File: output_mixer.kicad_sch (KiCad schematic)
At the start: 112 parts, among them J1 Conn_01x10, J11 IN2, J2 IN1, J3 IN1, J4 IN2, J5 Line out, J6 Headphones, Q2 BD139, Q3 BD140, Q4 BD139, Q5 BD140, U1 TL072, U2 TL072, U3 TL072

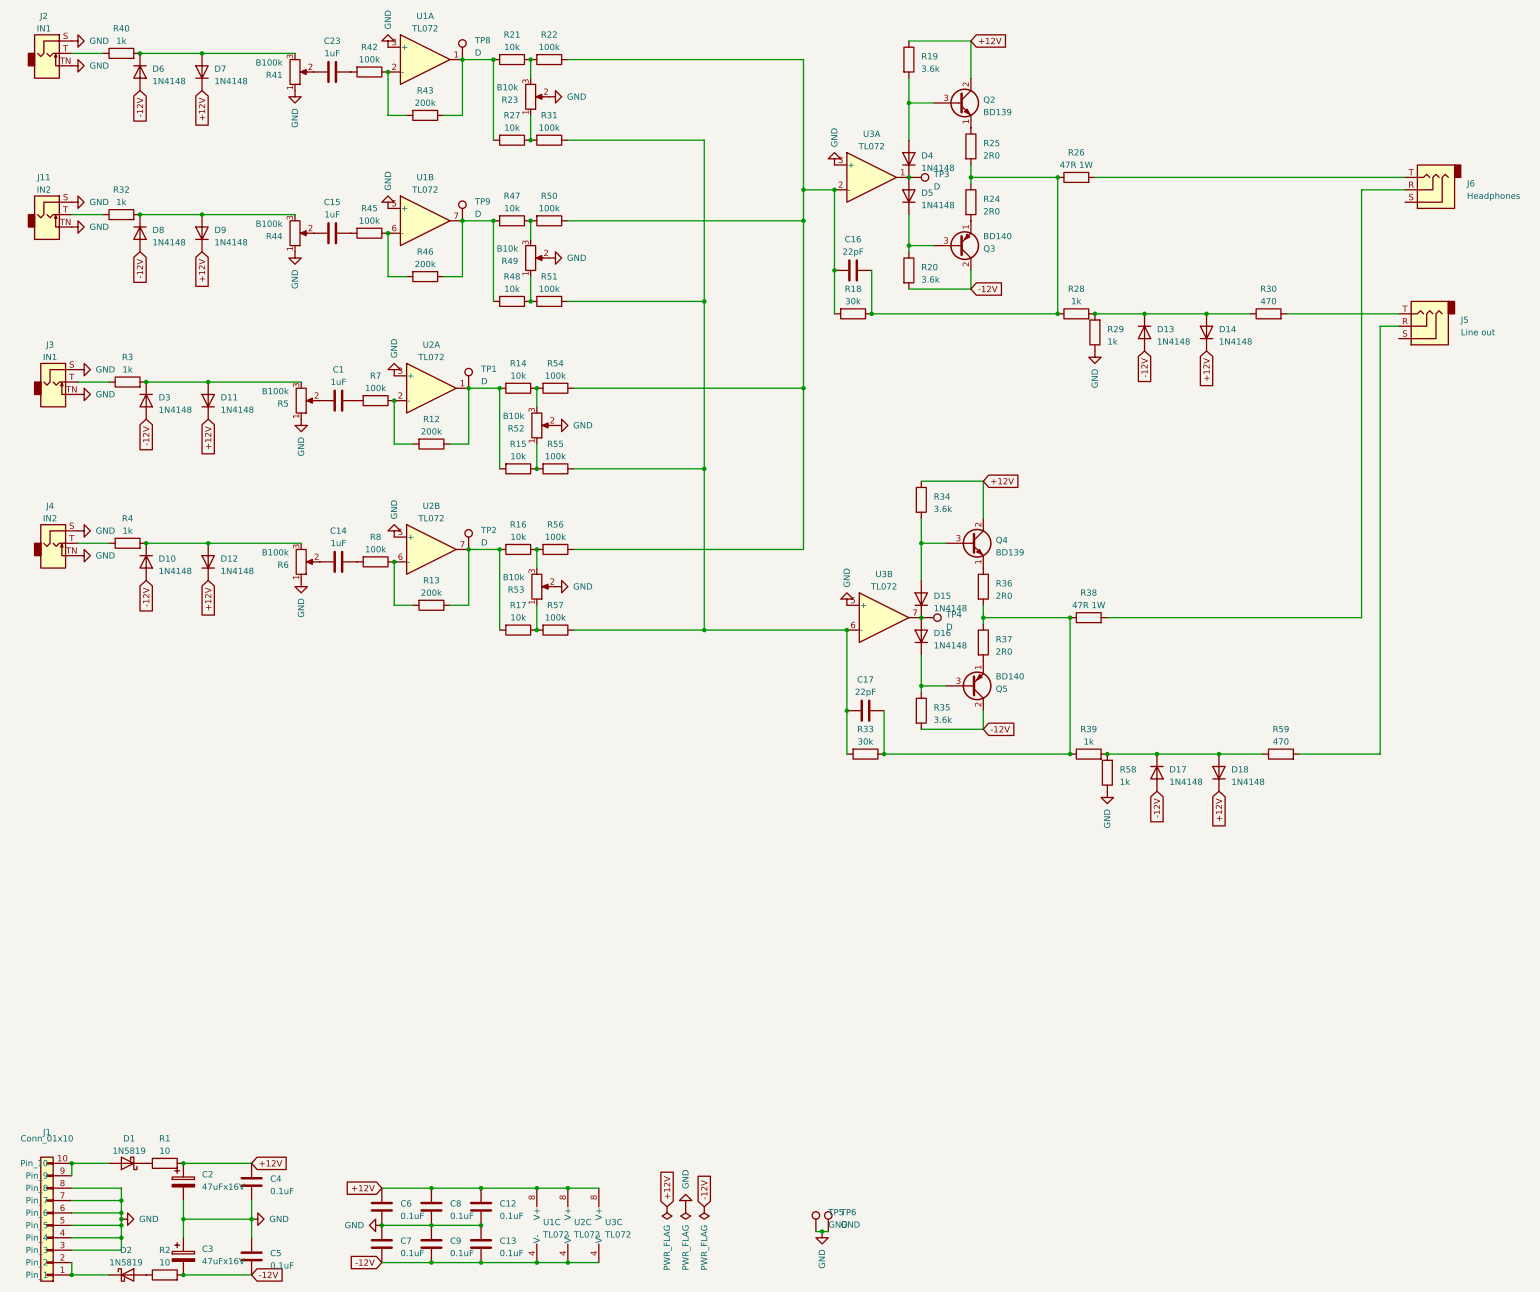
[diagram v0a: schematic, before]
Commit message: schematic done, some parts added to PCB
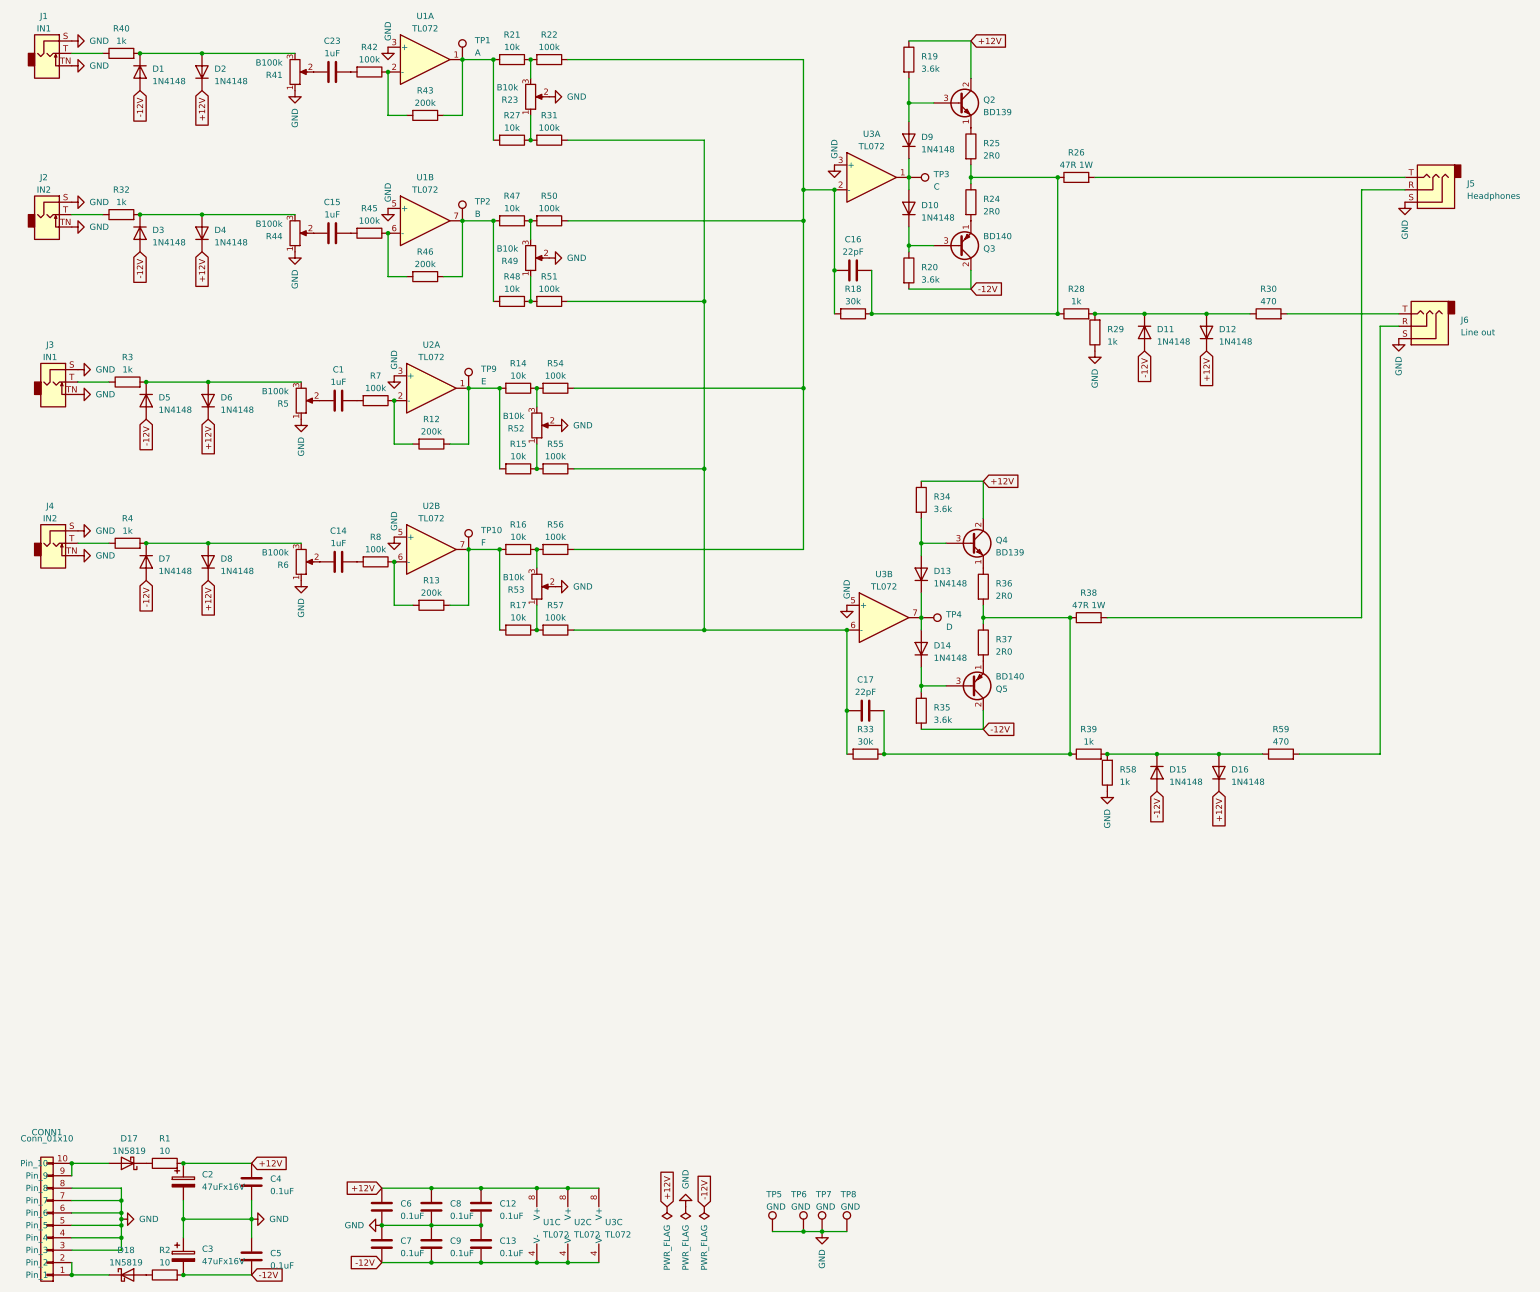
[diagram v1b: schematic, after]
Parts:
- added TP7, TP8: GND, TestPoint:TestPoint_THTPad_D2.5mm_Drill1.2mm, symbol Connector:TestPoint
- C1, C12, C13, C14, C15, C16, C17, C23, C4, C5, C6, C7, C8, C9: footprint Capacitor_THT:C_Disc_D5.0mm_W2.5mm_P5.00mm -> Capacitor_SMD:C_0603_1608Metric
- D1: renamed from D6; footprint Diode_THT:D_DO-35_SOD27_P7.62mm_Horizontal -> Diode_SMD:D_SOD-123
- D10: renamed from D5; footprint Diode_THT:D_DO-35_SOD27_P7.62mm_Horizontal -> Diode_SMD:D_SOD-123
- D11: renamed from D13; footprint Diode_THT:D_DO-35_SOD27_P7.62mm_Horizontal -> Diode_SMD:D_SOD-123
- D12: renamed from D14; footprint Diode_THT:D_DO-35_SOD27_P7.62mm_Horizontal -> Diode_SMD:D_SOD-123
- D13: renamed from D15; footprint Diode_THT:D_DO-35_SOD27_P7.62mm_Horizontal -> Diode_SMD:D_SOD-123
- D14: renamed from D16; footprint Diode_THT:D_DO-35_SOD27_P7.62mm_Horizontal -> Diode_SMD:D_SOD-123
- D15: renamed from D17; footprint Diode_THT:D_DO-35_SOD27_P7.62mm_Horizontal -> Diode_SMD:D_SOD-123
- D16: renamed from D18; footprint Diode_THT:D_DO-35_SOD27_P7.62mm_Horizontal -> Diode_SMD:D_SOD-123
- D17: renamed from D1; footprint Diode_THT:D_DO-41_SOD81_P7.62mm_Horizontal -> Diode_SMD:D_SOD-323
- D18: renamed from D2; footprint Diode_THT:D_DO-41_SOD81_P7.62mm_Horizontal -> Diode_SMD:D_SOD-323
- D2: renamed from D7; footprint Diode_THT:D_DO-35_SOD27_P7.62mm_Horizontal -> Diode_SMD:D_SOD-123
- D3: renamed from D8; footprint Diode_THT:D_DO-35_SOD27_P7.62mm_Horizontal -> Diode_SMD:D_SOD-123
- D4: renamed from D9; footprint Diode_THT:D_DO-35_SOD27_P7.62mm_Horizontal -> Diode_SMD:D_SOD-123
- D5: renamed from D3; footprint Diode_THT:D_DO-35_SOD27_P7.62mm_Horizontal -> Diode_SMD:D_SOD-123
- D6: renamed from D11; footprint Diode_THT:D_DO-35_SOD27_P7.62mm_Horizontal -> Diode_SMD:D_SOD-123
- D7: renamed from D10; footprint Diode_THT:D_DO-35_SOD27_P7.62mm_Horizontal -> Diode_SMD:D_SOD-123
- D8: renamed from D12; footprint Diode_THT:D_DO-35_SOD27_P7.62mm_Horizontal -> Diode_SMD:D_SOD-123
- D9: renamed from D4; footprint Diode_THT:D_DO-35_SOD27_P7.62mm_Horizontal -> Diode_SMD:D_SOD-123
- J5: renamed from J6; footprint (none) -> Connector_Audio:Jack_3.5mm_QingPu_WQP-PJ398SM_Vertical_CircularHoles_Stereo
- J6: renamed from J5; footprint (none) -> Connector_Audio:Jack_3.5mm_QingPu_WQP-PJ398SM_Vertical_CircularHoles_Stereo
- R1, R2, R24, R25, R26, R36, R37, R38: footprint Resistor_THT:R_Axial_DIN0207_L6.3mm_D2.5mm_P2.54mm_Vertical -> Resistor_THT:R_Axial_DIN0207_L6.3mm_D2.5mm_P7.62mm_Horizontal
- R12, R13, R14, R15, R16, R17, R18, R21, R22, R27, R28, R29, R3, R30, R31, R32, R33, R39, R4, R40, R42, R43, R45, R46, R47, R48, R50, R51, R54, R55, R56, R57, R58, R59, R7, R8: footprint Resistor_THT:R_Axial_DIN0207_L6.3mm_D2.5mm_P2.54mm_Vertical -> Resistor_SMD:R_0805_2012Metric
- R19, R20, R34, R35: footprint Resistor_THT:R_Axial_DIN0207_L6.3mm_D2.5mm_P2.54mm_Vertical -> Resistor_SMD:R_0603_1608Metric
- TP1: renamed from TP8; value D -> A; footprint Connector_PinSocket_1.27mm:PinSocket_1x01_P1.27mm_Vertical -> TestPoint:TestPoint_THTPad_D2.5mm_Drill1.2mm
- TP10: renamed from TP2; value D -> F; footprint Connector_PinSocket_1.27mm:PinSocket_1x01_P1.27mm_Vertical -> TestPoint:TestPoint_THTPad_D2.5mm_Drill1.2mm
- TP2: renamed from TP9; value D -> B; footprint Connector_PinSocket_1.27mm:PinSocket_1x01_P1.27mm_Vertical -> TestPoint:TestPoint_THTPad_D2.5mm_Drill1.2mm
- TP3: value D -> C; footprint Connector_PinSocket_1.27mm:PinSocket_1x01_P1.27mm_Vertical -> TestPoint:TestPoint_THTPad_D2.5mm_Drill1.2mm
- TP4, TP5, TP6: footprint Connector_PinSocket_1.27mm:PinSocket_1x01_P1.27mm_Vertical -> TestPoint:TestPoint_THTPad_D2.5mm_Drill1.2mm
- TP9: renamed from TP1; value D -> E; footprint Connector_PinSocket_1.27mm:PinSocket_1x01_P1.27mm_Vertical -> TestPoint:TestPoint_THTPad_D2.5mm_Drill1.2mm
- U1, U2, U3: footprint (none) -> Package_SO:SOP-8_3.9x4.9mm_P1.27mm
- renumbered J1 to CONN1, J2 to J1, J11 to J2
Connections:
- net GND: now also J5.S, J6.S, TP7.1, TP8.1
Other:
- moved on the sheet: D10, D13, D14, D9, TP5, TP6
